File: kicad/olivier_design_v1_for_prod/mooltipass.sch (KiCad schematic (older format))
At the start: 65 parts, among them CON2 CON_10118194-0001LF, P1 CONN_8, P2 CONN_6, P3 CONN_10, P4 CONN_8, P5 CONN_1, P6 CONN_1, P7 CONN_1, P8 CONN_1, Q1 MOS_P, Q2 MOS_N, Q3 MOS_P, Q4 MOS_N, U1 CON_SFV30R-2STE1HLF, U2 CON_7312P0225A13LF, U3 IP4234CZ6,125, U4 ATMEGA32U4_QFN, U5 ST662ACD, U6 AT45DB011D-SSH, U7 CON_STACK_9, X1 16MHz

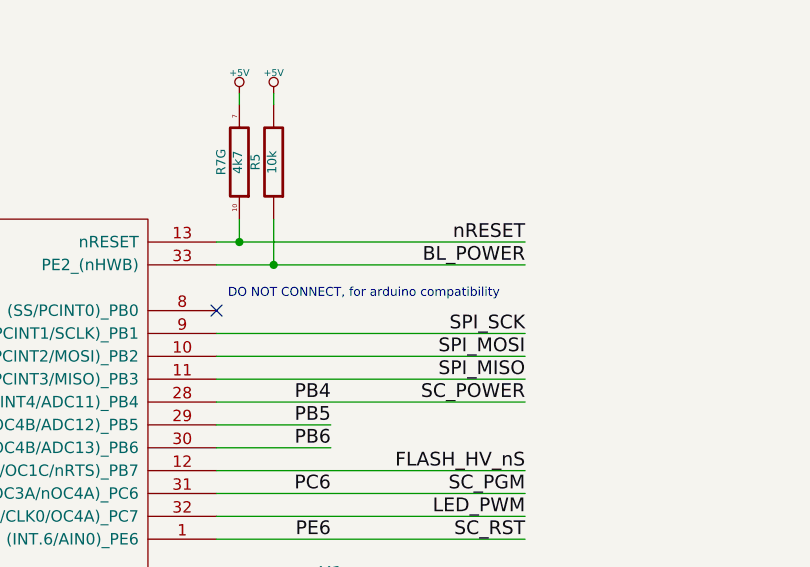
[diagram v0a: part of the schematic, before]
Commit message: adding a 10k resistor for oled power mosp
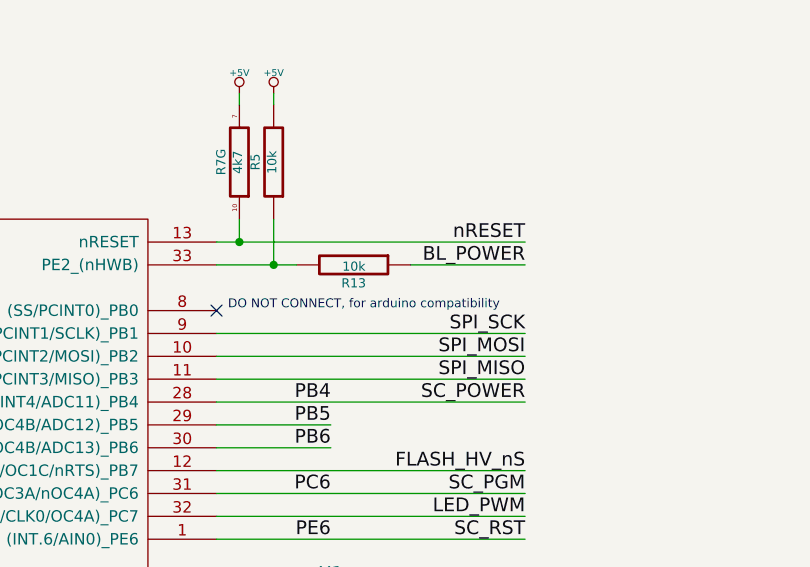
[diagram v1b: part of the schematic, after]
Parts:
- added R13: 10k, ~, symbol R
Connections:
- net BL_POWER: now also R13.1; no longer R5.1, U4.33 (PE2_(nHWB))
- new net: R13.2, R5.1, U4.33 (PE2_(nHWB))
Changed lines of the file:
@@
 Sheet 1 1
 Title "M. Stephan - Mooltipass Schematics (Licensed under CERN OHL V1.2)"
-Date "25 jun 2014"
+Date "15 feb 2015"
 Rev "2"
 Comp ""
@@
 $EndComp
 NoConn ~ 11450 5900
-Text Notes 11500 5850 0    39   ~ 0
+Text Notes 11500 5900 0    39   ~ 0
 DO NOT CONNECT, for arduino compatibility
 $Comp
@@
 	11450 6800 12800 6800
 Wire Wire Line
-	11450 5700 12800 5700
-Wire Wire Line
 	11700 5700 11700 5500
 Connection ~ 11700 5700
@@
 	5750 1050 5750 1000
 Connection ~ 5450 1250
+$Comp
+L R R13
+U 1 1 54E09BC6
+P 12050 5700
+F 0 "R13" V 12130 5700 40  0000 C CNN
+F 1 "10k" V 12057 5701 40  0000 C CNN
+F 2 "~" V 11980 5700 30  0000 C CNN
+F 3 "~" H 12050 5700 30  0000 C CNN
+	1    12050 5700
+	0    1    1    0
+$EndComp
+Wire Wire Line
+	11450 5700 11800 5700
+Wire Wire Line
+	12300 5700 12800 5700
 $EndSCHEMATC
